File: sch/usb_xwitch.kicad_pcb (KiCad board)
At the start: 2 copper layers, 65 x 56.5 mm, 62 parts, among them J1 USB3_A, J2 USB3_A, J3 USB3_A, J4 USB3_A, J5 USB3_A, J6 USB3_A, J7 USB3_A, J8 Conn_02x05_Odd_Even, J9 Conn_02x03_Odd_Even, K1 Relay_DPDT_Panasonic_AGQ200A4H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

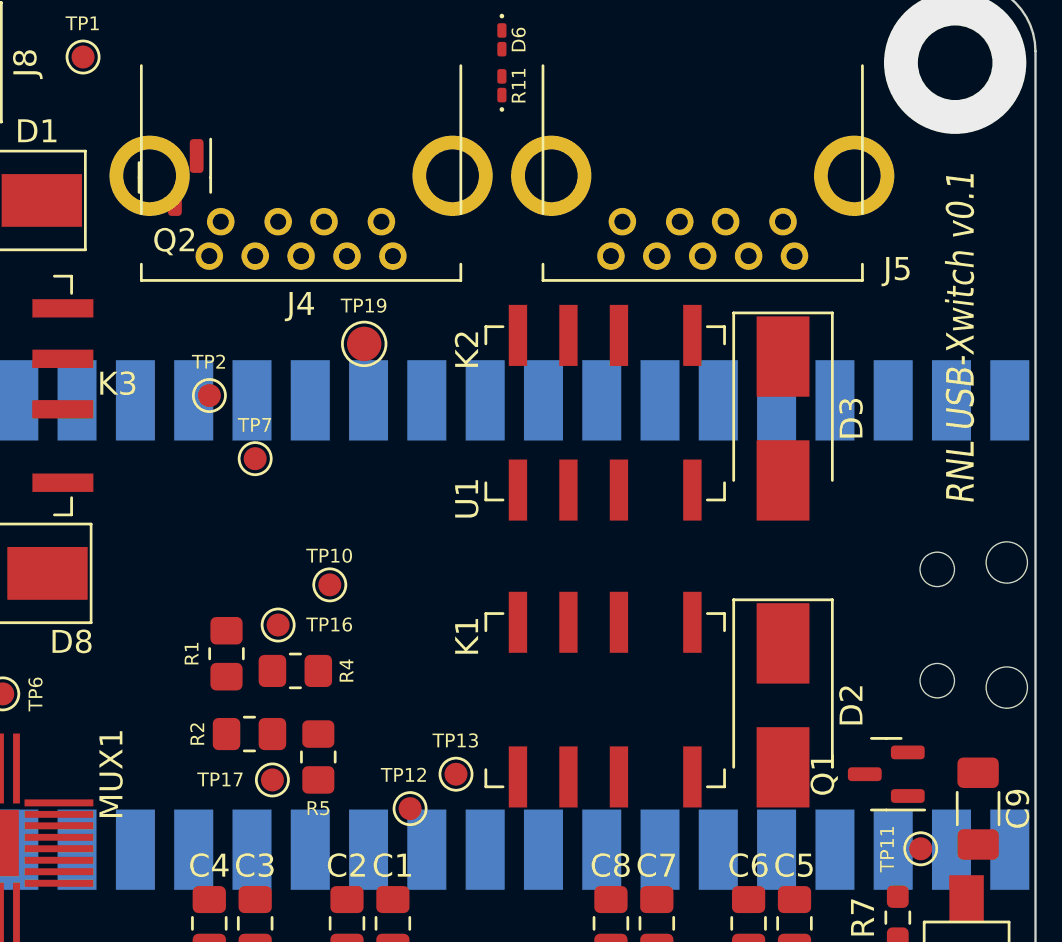
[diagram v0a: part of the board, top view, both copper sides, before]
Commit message: fixed q2 not placed properly
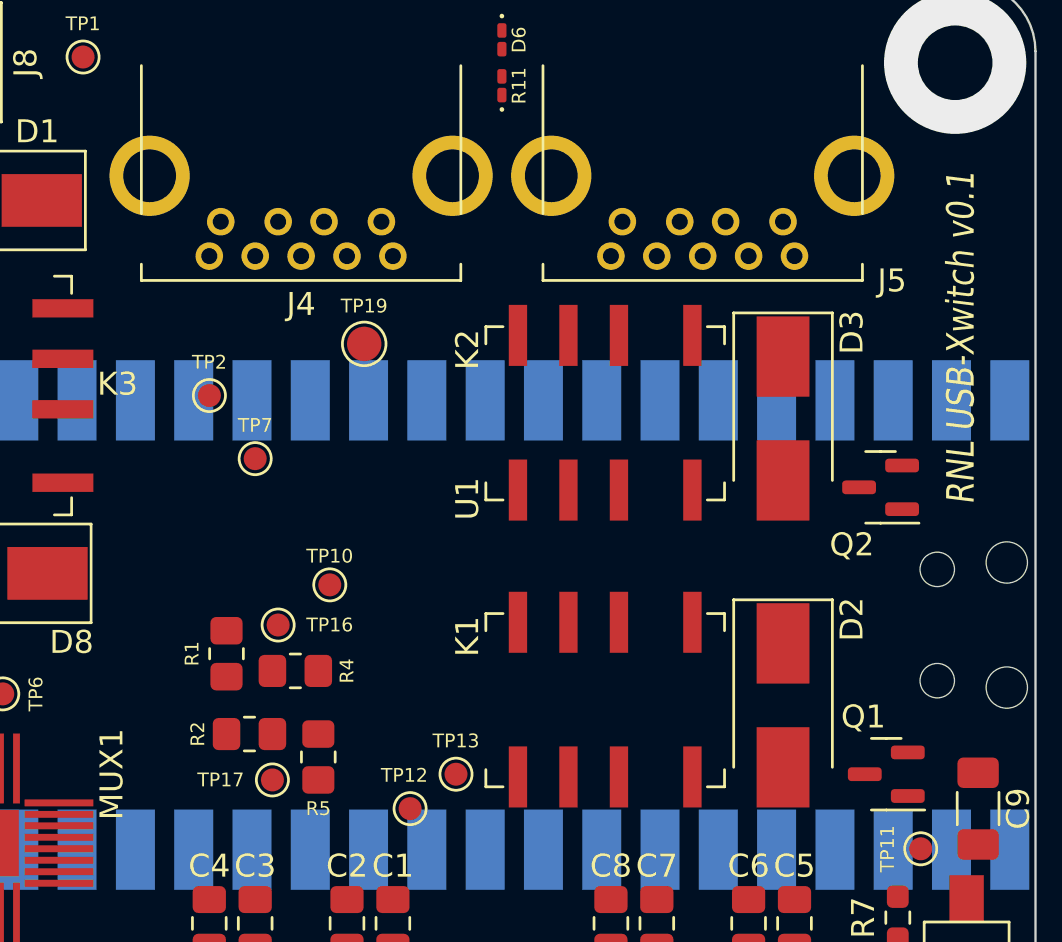
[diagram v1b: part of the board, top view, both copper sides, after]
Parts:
- moved Q2 33.6 mm to (158.2, 102.0), turned to 180 degrees
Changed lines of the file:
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@@
     (property "Sheetname" "")
     (attr through_hole)
-    (fp_text reference "J5" (at -5 -2.075) (layer "F.SilkS")
+    (fp_text reference "J5" (at -4.75 -2.575) (layer "F.SilkS")
       (effects (font (size 1 1) (thickness 0.15)))
     )
@@
     (property "Sheetname" "")
     (attr smd)
-    (fp_text reference "D2" (at 0 -3 -90) (layer "F.SilkS")
+    (fp_text reference "D2" (at -3.75 -3 -90) (layer "F.SilkS")
       (effects (font (size 1 1) (thickness 0.15)))
     )
@@
   )
   (footprint "Package_TO_SOT_SMD:SOT-23" (layer "F.Cu")
-    (at 127.5 88.5 -90)
+    (at 158.25 102 180)
     (descr "SOT, 3 Pin (https://www.jedec.org/system/files/docs/to-236h.pdf variant AB), generated with kicad-footprint-generator ipc_gullwing_generator.py")
     (tags "SOT TO_SOT_SMD")
@@
     (property "Sheetname" "")
     (attr smd)
-    (fp_text reference "Q2" (at 2.75 0) (layer "F.SilkS")
-      (effects (font (size 1 1) (thickness 0.15)))
-    )
-    (fp_text value "2N7002P" (at 0 2.4 90) (layer "F.Fab") hide
-      (effects (font (size 1 1) (thickness 0.15)))
-    )
-    (fp_text user "${REFERENCE}" (at 0 0 90) (layer "F.Fab") hide
+    (fp_text reference "Q2" (at 1.25 -2.5 180) (layer "F.SilkS")
+      (effects (font (size 1 1) (thickness 0.15)))
+    )
+    (fp_text value "2N7002P" (at 0 2.4) (layer "F.Fab") hide
+      (effects (font (size 1 1) (thickness 0.15)))
+    )
+    (fp_text user "${REFERENCE}" (at 0 0) (layer "F.Fab") hide
       (effects (font (size 0.32 0.32) (thickness 0.05)))
     )
@@
     (fp_line (start -0.65 -1.125) (end -0.325 -1.45) (layer "F.Fab") (width 0.1))
     (fp_line (start 0.65 -1.45) (end 0.65 1.45) (layer "F.Fab") (width 0.1))
-    (pad "1" smd roundrect (at -0.9375 -0.95 270) (size 1.475 0.6) (layers "F.Cu" "F.Paste" "F.Mask") (roundrect_rratio 0.25)
+    (pad "1" smd roundrect (at -0.9375 -0.95 180) (size 1.475 0.6) (layers "F.Cu" "F.Paste" "F.Mask") (roundrect_rratio 0.25)
       (net 71 "/REL-B") (pinfunction "G") (pintype "input"))
-    (pad "2" smd roundrect (at -0.9375 0.95 270) (size 1.475 0.6) (layers "F.Cu" "F.Paste" "F.Mask") (roundrect_rratio 0.25)
+    (pad "2" smd roundrect (at -0.9375 0.95 180) (size 1.475 0.6) (layers "F.Cu" "F.Paste" "F.Mask") (roundrect_rratio 0.25)
       (net 17 "GND") (pinfunction "S") (pintype "passive"))
-    (pad "3" smd roundrect (at 0.9375 0 270) (size 1.475 0.6) (layers "F.Cu" "F.Paste" "F.Mask") (roundrect_rratio 0.25)
+    (pad "3" smd roundrect (at 0.9375 0 180) (size 1.475 0.6) (layers "F.Cu" "F.Paste" "F.Mask") (roundrect_rratio 0.25)
       (net 38 "/RL2") (pinfunction "D") (pintype "passive"))
     (model "${KICAD6_3DMODEL_DIR}/Package_TO_SOT_SMD.3dshapes/SOT-23.wrl"
@@
     (property "Sheetname" "")
     (attr smd)
-    (fp_text reference "Q1" (at 2.75 0 90) (layer "F.SilkS")
+    (fp_text reference "Q1" (at 1 2.5 180) (layer "F.SilkS")
       (effects (font (size 1 1) (thickness 0.15)))
     )
@@
     (property "Sheetname" "")
     (attr smd)
-    (fp_text reference "D3" (at 0 -3 -90) (layer "F.SilkS")
-      (effects (font (size 1 1) (thickness 0.15)))
-    )
+    (fp_text reference "D3" (at -3.75 -3 -90) (layer "F.SilkS")
+      (effects (font (size 1 1) (thickness 0.15)))
+    )

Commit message: pcb updated
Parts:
- moved C1 7.22 mm to (130.0, 119.2)
- moved C4 7.22 mm to (136.0, 119.2)
- moved TP8 3.91 mm to (117.0, 113.8)
- moved C2 3.47 mm to (132.0, 119.2)
- moved C3 3.47 mm to (134.0, 119.2)
- moved TP3 3.29 mm to (118.5, 113.8)
- moved TP9 1.00 mm to (116.2, 120.2)
- moved JP1 0.50 mm to (126.8, 134.5)
- moved JP2 0.50 mm to (126.8, 132.0)
- turned C7 to -90 degrees
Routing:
- net Net-(C5-Pad1): track 0.00 -> 38.7 mm, vias 0 -> 2
- net Net-(C6-Pad1): track 0.00 -> 36.9 mm, vias 0 -> 2
- net /TX+BP: track 0.00 -> 35.7 mm, vias 0 -> 1
- net Net-(C7-Pad1): track 0.00 -> 31.9 mm, vias 0 -> 2
- net /TX-BP: track 0.00 -> 31.9 mm, vias 0 -> 1
- net Net-(C8-Pad1): track 0.00 -> 28.5 mm, vias 0 -> 2
- net /TX+BP1: track 0.00 -> 28.1 mm
- net /TX-BP1: track 0.00 -> 27.5 mm, vias 0 -> 1
- net /RX+BP: track 0.00 -> 27.5 mm
- net /RX-BP: track 0.00 -> 26.1 mm
- net Net-(J1-Pad2): track 0.00 -> 23.0 mm, vias 0 -> 1
- net Net-(J1-Pad3): track 0.00 -> 22.6 mm
- net /SEL-A: track 0.00 -> 16.7 mm, vias 0 -> 1
- net Net-(C4-Pad1): track 0.00 -> 15.4 mm
- net Net-(C3-Pad1): track 0.00 -> 13.4 mm
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
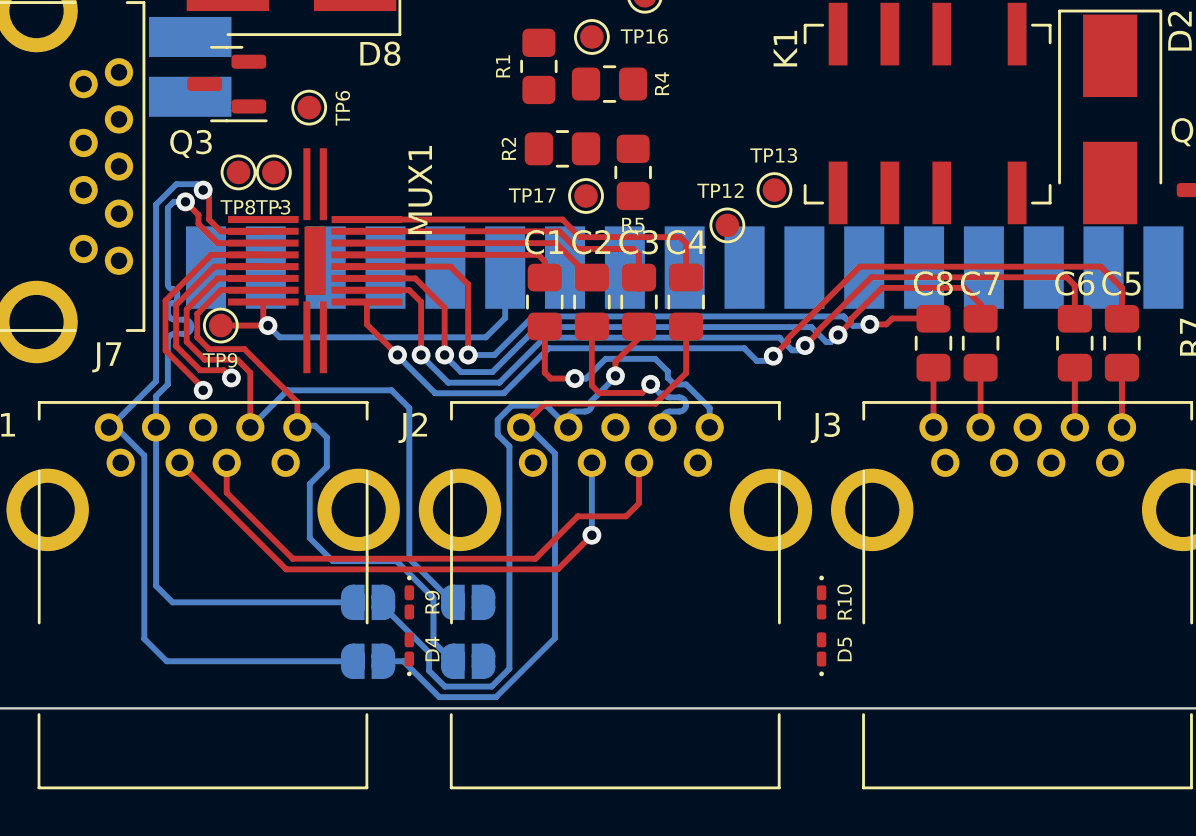
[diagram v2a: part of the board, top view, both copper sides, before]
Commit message: usb gnd changed; wired mux1 all parts
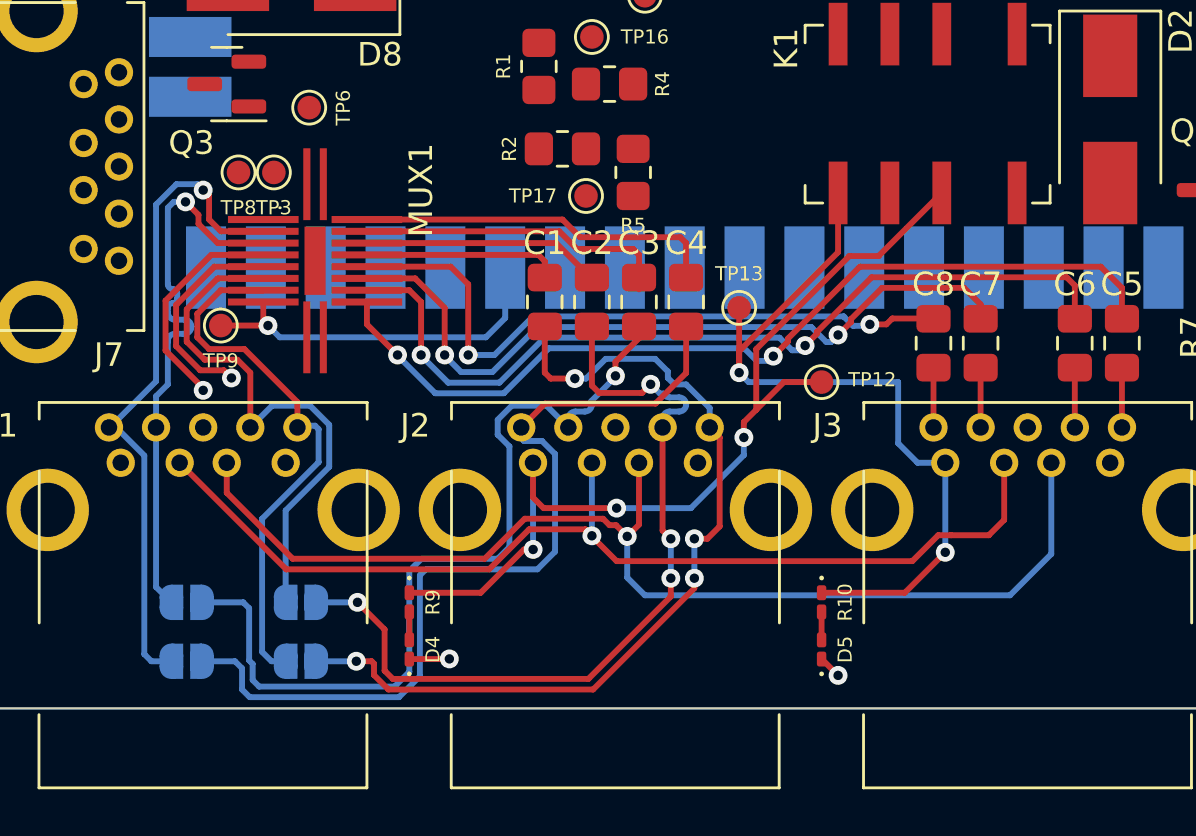
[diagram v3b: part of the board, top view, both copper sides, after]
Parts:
- moved TP12 7.76 mm to (141.8, 122.7)
- moved JP3 7.70 mm to (114.8, 132.0)
- moved JP4 7.70 mm to (114.8, 134.5)
- moved JP1 7.10 mm to (119.7, 134.5)
- moved JP2 7.10 mm to (119.7, 132.0)
- moved TP13 5.22 mm to (138.2, 119.5)
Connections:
- J2 pad 10: Net-(J2-Pad10) -> GND
- J2 pad 4: Net-(J2-Pad10) -> GND
- J2 pad 7: Net-(J2-Pad10) -> GND
- J3 pad 10: Net-(J3-Pad10) -> GND
- J3 pad 4: Net-(J3-Pad10) -> GND
- J3 pad 7: Net-(J3-Pad10) -> GND
- J5 pad 10: Net-(J5-Pad10) -> GND
- J5 pad 4: Net-(J5-Pad10) -> GND
- J5 pad 7: Net-(J5-Pad10) -> GND
- J7 pad 10: Net-(J7-Pad10) -> GND
- J7 pad 4: Net-(J7-Pad10) -> GND
- J7 pad 7: Net-(J7-Pad10) -> GND
- K1 pad 2: Net-(J2-Pad10) -> unconnected-(K1-Pad2)
- K1 pad 3: GND -> unconnected-(K1-Pad3)
- K1 pad 4: Net-(J3-Pad10) -> unconnected-(K1-Pad4)
- K2 pad 2: Net-(J5-Pad10) -> unconnected-(K2-Pad2)
- K2 pad 3: GND -> unconnected-(K2-Pad3)
- K3 pad 2: Net-(J7-Pad10) -> unconnected-(K3-Pad2)
- K3 pad 3: GND -> unconnected-(K3-Pad3)
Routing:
- net /VBUS_1_1: track 0.00 -> 39.8 mm, vias 0 -> 3
- net /VBUS_1_2: track 0.00 -> 33.7 mm, vias 0 -> 2
- net /RX-BP1: track 11.3 -> 37.6 mm, vias 1 -> 4
- net /RX+BP1: track 8.37 -> 34.6 mm, vias 1 -> 4
- net Net-(J1-Pad3): track 22.6 -> 48.4 mm, vias 0 -> 1
- net Net-(J1-Pad2): track 23.0 -> 44.4 mm
- net /TX+BP1: track 28.1 -> 37.0 mm
- net /TX-BP1: track 27.5 -> 35.8 mm
- net /TX-BP: track 31.9 -> 24.2 mm
- net /TX+BP: track 35.7 -> 28.3 mm
- net /RX+BP: track 27.5 -> 23.1 mm
- net /RX-BP: track 26.1 -> 23.3 mm
- net GND: track 9.75 -> 12.4 mm, vias 1 -> 3
- net Net-(D5-Pad2): track 0.00 -> 1.19 mm
- net Net-(D4-Pad2): track 0.00 -> 1.19 mm

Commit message: pcb in progress
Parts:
- moved TP7 11.0 mm to (141.3, 104.7)
- moved TP10 9.20 mm to (127.5, 112.5)
- moved R2 7.14 mm to (134.1, 106.5)
- moved R5 7.14 mm to (137.1, 107.5)
- moved TP17 7.14 mm to (135.1, 108.5)
- moved R1 6.77 mm to (133.2, 103.4)
- moved R4 6.77 mm to (136.2, 104.2)
- moved TP16 6.77 mm to (135.4, 102.2)
- moved TP19 2.65 mm to (135.6, 98.4)
- moved TP13 1.40 mm to (138.2, 118.1)
- moved TP8 0.91 mm to (116.8, 112.8)
- moved TP6 0.74 mm to (119.7, 110.3)
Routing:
- net +5V: track 0.00 -> 136.2 mm, vias 0 -> 1
- net +3V3: track 9.03 -> 101.6 mm, vias 1 -> 4
- net /UART_PI_TX: track 0.00 -> 90.2 mm, vias 0 -> 1
- net /UART_PI_RX: track 0.00 -> 86.9 mm, vias 0 -> 1
- net Net-(J1-Pad1): track 0.00 -> 57.4 mm, vias 0 -> 2
- net /REL-A: track 0.00 -> 43.8 mm, vias 0 -> 1
- net /VBUS2: track 0.00 -> 33.4 mm, vias 0 -> 2
- net /REL-B: track 0.00 -> 33.2 mm, vias 0 -> 1
- net Net-(J4-Pad5): track 0.00 -> 28.1 mm
- net /VBUS_1_1: track 39.8 -> 67.7 mm
- net Net-(J4-Pad6): track 0.00 -> 27.6 mm, vias 0 -> 1
- net Net-(J4-Pad3): track 0.00 -> 22.2 mm
- net Net-(J4-Pad2): track 0.00 -> 22.1 mm
- net Net-(J4-Pad9): track 0.00 -> 22.1 mm
- net Net-(J4-Pad8): track 0.00 -> 21.7 mm, vias 0 -> 1
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
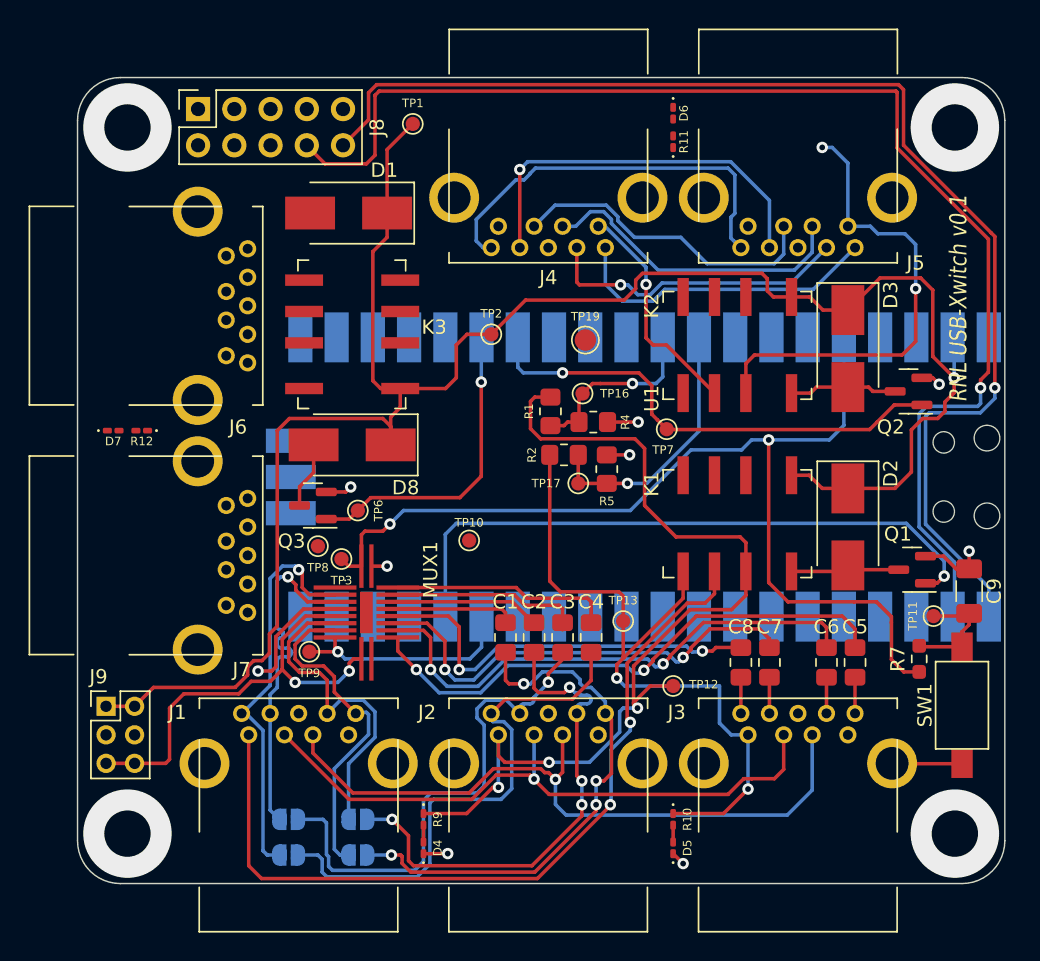
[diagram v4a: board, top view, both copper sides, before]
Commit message: pcb routed exc gnd
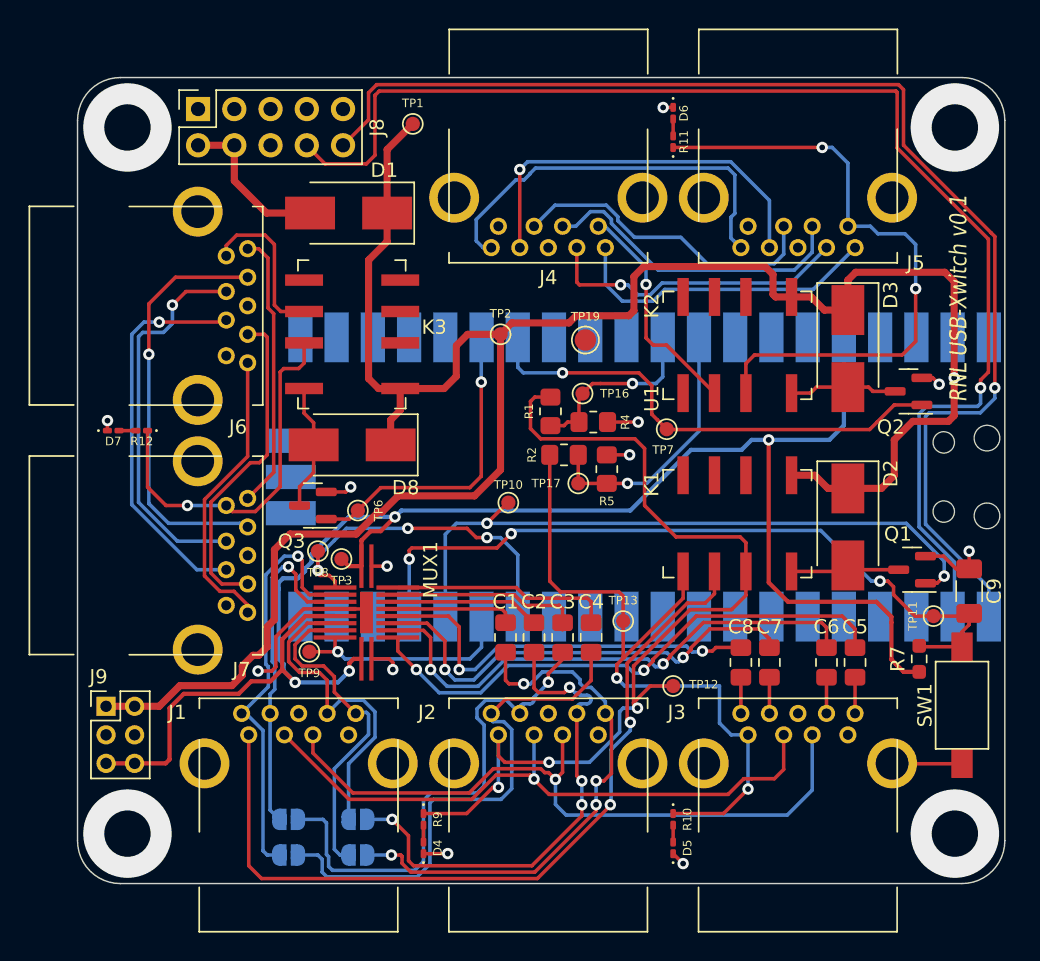
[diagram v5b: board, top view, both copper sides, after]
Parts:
- moved TP10 3.82 mm to (130.2, 109.8)
- moved TP2 0.65 mm to (129.7, 98.0)
- moved TP8 0.35 mm to (116.8, 113.2)
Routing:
- net /SW-A: track 8.15 -> 52.0 mm, vias 0 -> 3
- net Net-(J6-Pad8): track 0.00 -> 29.3 mm, vias 0 -> 1
- net Net-(J6-Pad3): track 0.00 -> 27.5 mm, vias 0 -> 1
- net Net-(J6-Pad2): track 0.00 -> 27.1 mm, vias 0 -> 1
- net /VBUS3: track 0.00 -> 26.1 mm, vias 0 -> 1
- net /PD-A: track 0.00 -> 23.4 mm, vias 0 -> 3
- net Net-(J6-Pad6): track 0.00 -> 22.9 mm
- net Net-(J6-Pad5): track 0.00 -> 20.6 mm
- net Net-(J6-Pad9): track 0.00 -> 19.5 mm
- net +3V3: track 101.6 -> 119.3 mm
- net +5V: track 136.2 -> 150.4 mm
- net Net-(D1-Pad2): track 0.00 -> 11.3 mm
- net Net-(J6-Pad1): track 0.00 -> 11.2 mm
- net /VBUS2: track 33.4 -> 43.8 mm
- net GND: track 29.1 -> 34.8 mm, vias 9 -> 12
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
